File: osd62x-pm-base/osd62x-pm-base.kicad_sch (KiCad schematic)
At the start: 0 parts

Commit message: Schematic update
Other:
- added sheet clocks & reset (clocksresets.kicad_sch)
- added sheet ddr & gpmc interface (ddr-gpmc.kicad_sch)
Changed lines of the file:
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@@
+		)
+	)
+	(sheet
+		(at 25.4 55.88)
+		(size 26.67 6.35)
+		(exclude_from_sim no)
+		(in_bom yes)
+		(on_board yes)
+		(dnp no)
+		(fields_autoplaced yes)
+		(stroke
+			(width 0.1524)
+			(type solid)
+		)
+		(fill
+			(color 0 0 0 0.0000)
+		)
+		(property "Sheetname" "ddr & gpmc interface"
+			(at 25.4 55.1684 0)
+			(effects
+				(font
+					(size 1.27 1.27)
+				)
+				(justify left bottom)
+			)
+		)
+		(property "Sheetfile" "ddr-gpmc.kicad_sch"
+			(at 25.4 62.8146 0)
+			(effects
+				(font
+					(size 1.27 1.27)
+				)
+				(justify left top)
+			)
+		)
+		(instances
+			(project "osd62x-pm-base"
+				(path "/45b90a68-cf5c-4d95-91b2-d04264fee060"
+					(page "4")
+				)
+			)
+		)
+	)
+	(sheet
+		(at 25.4 43.18)
+		(size 26.67 6.35)
+		(exclude_from_sim no)
+		(in_bom yes)
+		(on_board yes)
+		(dnp no)
+		(fields_autoplaced yes)
+		(stroke
+			(width 0.1524)
+			(type solid)
+		)
+		(fill
+			(color 0 0 0 0.0000)
+		)
+		(property "Sheetname" "clocks & reset"
+			(at 25.4 42.4684 0)
+			(effects
+				(font
+					(size 1.27 1.27)
+				)
+				(justify left bottom)
+			)
+		)
+		(property "Sheetfile" "clocksresets.kicad_sch"
+			(at 25.4 50.1146 0)
+			(effects
+				(font
+					(size 1.27 1.27)
+				)
+				(justify left top)
+			)
+		)
+		(instances
+			(project "osd62x-pm-base"
+				(path "/45b90a68-cf5c-4d95-91b2-d04264fee060"
+					(page "3")
+				)
+			)
 		)
 	)

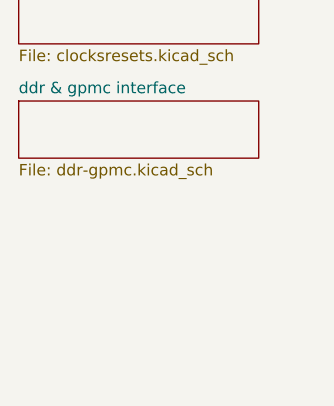
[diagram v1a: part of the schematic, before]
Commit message: Unit D created and peripherals page added
Created unit D and added peripherals schematic page
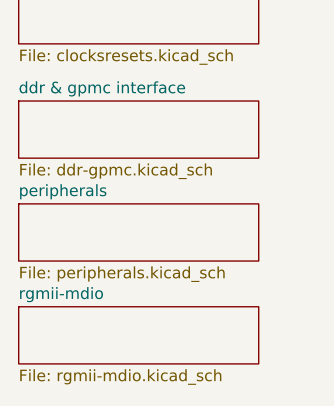
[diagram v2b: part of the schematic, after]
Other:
- added sheet peripherals (peripherals.kicad_sch)
- added sheet rgmii-mdio (rgmii-mdio.kicad_sch)
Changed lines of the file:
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@@
+		)
+	)
+	(sheet
+		(at 25.4 67.31)
+		(size 26.67 6.35)
+		(exclude_from_sim no)
+		(in_bom yes)
+		(on_board yes)
+		(dnp no)
+		(fields_autoplaced yes)
+		(stroke
+			(width 0.1524)
+			(type solid)
+		)
+		(fill
+			(color 0 0 0 0.0000)
+		)
+		(property "Sheetname" "peripherals"
+			(at 25.4 66.5984 0)
+			(effects
+				(font
+					(size 1.27 1.27)
+				)
+				(justify left bottom)
+			)
+		)
+		(property "Sheetfile" "peripherals.kicad_sch"
+			(at 25.4 74.2446 0)
+			(effects
+				(font
+					(size 1.27 1.27)
+				)
+				(justify left top)
+			)
+		)
+		(instances
+			(project "osd62x-pm-base"
+				(path "/45b90a68-cf5c-4d95-91b2-d04264fee060"
+					(page "5")
+				)
+			)
+		)
+	)
+	(sheet
+		(at 25.4 78.74)
+		(size 26.67 6.35)
+		(exclude_from_sim no)
+		(in_bom yes)
+		(on_board yes)
+		(dnp no)
+		(fields_autoplaced yes)
+		(stroke
+			(width 0.1524)
+			(type solid)
+		)
+		(fill
+			(color 0 0 0 0.0000)
+		)
+		(property "Sheetname" "rgmii-mdio"
+			(at 25.4 78.0284 0)
+			(effects
+				(font
+					(size 1.27 1.27)
+				)
+				(justify left bottom)
+			)
+		)
+		(property "Sheetfile" "rgmii-mdio.kicad_sch"
+			(at 25.4 85.6746 0)
+			(effects
+				(font
+					(size 1.27 1.27)
+				)
+				(justify left top)
+			)
+		)
+		(instances
+			(project "osd62x-pm-base"
+				(path "/45b90a68-cf5c-4d95-91b2-d04264fee060"
+					(page "6")
+				)
+			)
 		)
 	)

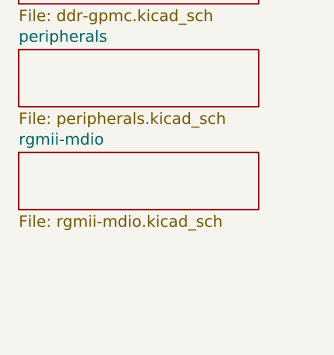
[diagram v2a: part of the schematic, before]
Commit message: Unit F created and placed.
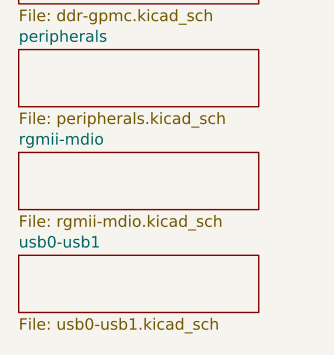
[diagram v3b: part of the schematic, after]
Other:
- added sheet usb0-usb1 (usb0-usb1.kicad_sch)
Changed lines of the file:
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@@
+	)
+	(sheet
+		(at 25.4 90.17)
+		(size 26.67 6.35)
+		(exclude_from_sim no)
+		(in_bom yes)
+		(on_board yes)
+		(dnp no)
+		(fields_autoplaced yes)
+		(stroke
+			(width 0.1524)
+			(type solid)
+		)
+		(fill
+			(color 0 0 0 0.0000)
+		)
+		(property "Sheetname" "usb0-usb1"
+			(at 25.4 89.4584 0)
+			(effects
+				(font
+					(size 1.27 1.27)
+				)
+				(justify left bottom)
+			)
+		)
+		(property "Sheetfile" "usb0-usb1.kicad_sch"
+			(at 25.4 97.1046 0)
+			(effects
+				(font
+					(size 1.27 1.27)
+				)
+				(justify left top)
+			)
+		)
+		(instances
+			(project "osd62x-pm-base"
+				(path "/45b90a68-cf5c-4d95-91b2-d04264fee060"
+					(page "7")
+				)
+			)
+		)
 	)
 	(sheet

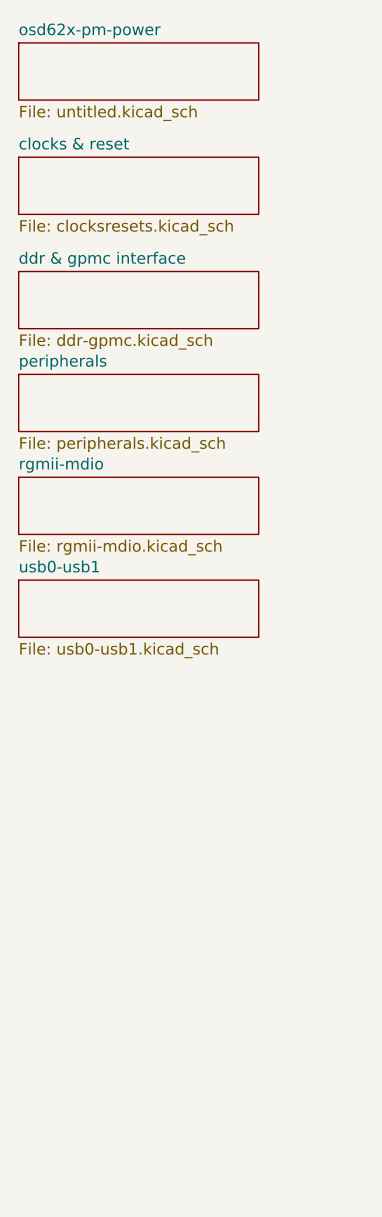
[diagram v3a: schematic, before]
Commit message: Unit G & H added
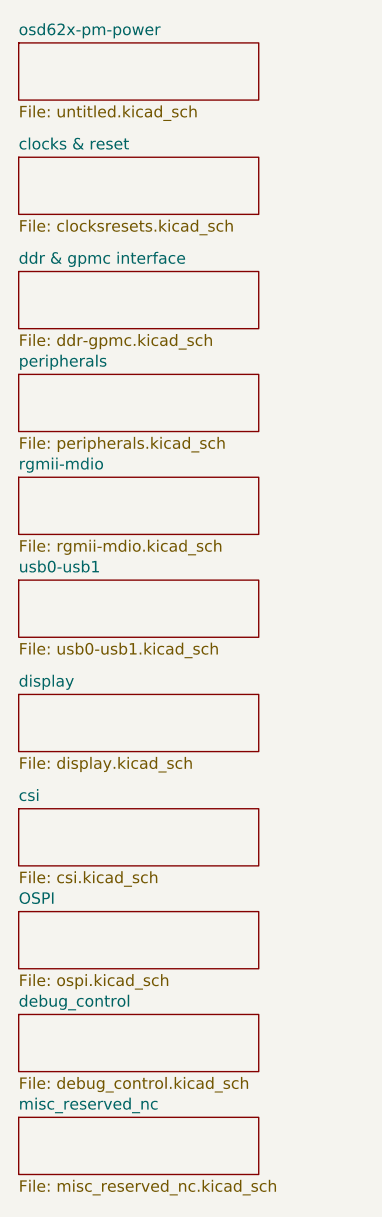
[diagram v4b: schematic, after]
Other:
- added sheet OSPI (ospi.kicad_sch)
- added sheet csi (csi.kicad_sch)
- added sheet debug_control (debug_control.kicad_sch)
- added sheet display (display.kicad_sch)
- added sheet misc_reserved_nc (misc_reserved_nc.kicad_sch)
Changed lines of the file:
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@@
+	)
+	(sheet
+		(at 25.4 115.57)
+		(size 26.67 6.35)
+		(exclude_from_sim no)
+		(in_bom yes)
+		(on_board yes)
+		(dnp no)
+		(fields_autoplaced yes)
+		(stroke
+			(width 0.1524)
+			(type solid)
+		)
+		(fill
+			(color 0 0 0 0.0000)
+		)
+		(property "Sheetname" "csi"
+			(at 25.4 114.8584 0)
+			(effects
+				(font
+					(size 1.27 1.27)
+				)
+				(justify left bottom)
+			)
+		)
+		(property "Sheetfile" "csi.kicad_sch"
+			(at 25.4 122.5046 0)
+			(effects
+				(font
+					(size 1.27 1.27)
+				)
+				(justify left top)
+			)
+		)
+		(instances
+			(project "osd62x-pm-base"
+				(path "/45b90a68-cf5c-4d95-91b2-d04264fee060"
+					(page "9")
+				)
+			)
+		)
+	)
+	(sheet
+		(at 25.4 102.87)
+		(size 26.67 6.35)
+		(exclude_from_sim no)
+		(in_bom yes)
+		(on_board yes)
+		(dnp no)
+		(fields_autoplaced yes)
+		(stroke
+			(width 0.1524)
+			(type solid)
+		)
+		(fill
+			(color 0 0 0 0.0000)
+		)
+		(property "Sheetname" "display"
+			(at 25.4 102.1584 0)
+			(effects
+				(font
+					(size 1.27 1.27)
+				)
+				(justify left bottom)
+			)
+		)
+		(property "Sheetfile" "display.kicad_sch"
+			(at 25.4 109.8046 0)
+			(effects
+				(font
+					(size 1.27 1.27)
+				)
+				(justify left top)
+			)
+		)
+		(instances
+			(project "osd62x-pm-base"
+				(path "/45b90a68-cf5c-4d95-91b2-d04264fee060"
+					(page "8")
+				)
+			)
+		)
 	)
 	(sheet
@@
 	)
 	(sheet
+		(at 25.4 138.43)
+		(size 26.67 6.35)
+		(exclude_from_sim no)
+		(in_bom yes)
+		(on_board yes)
+		(dnp no)
+		(fields_autoplaced yes)
+		(stroke
+			(width 0.1524)
+			(type solid)
+		)
+		(fill
+			(color 0 0 0 0.0000)
+		)
+		(property "Sheetname" "debug_control"
+			(at 25.4 137.7184 0)
+			(effects
+				(font
+					(size 1.27 1.27)
+				)
+				(justify left bottom)
+			)
+		)
+		(property "Sheetfile" "debug_control.kicad_sch"
+			(at 25.4 145.3646 0)
+			(effects
+				(font
+					(size 1.27 1.27)
+				)
+				(justify left top)
+			)
+		)
+		(instances
+			(project "osd62x-pm-base"
+				(path "/45b90a68-cf5c-4d95-91b2-d04264fee060"
+					(page "11")
+				)
+			)
+		)
+	)
+	(sheet
+		(at 25.4 149.86)
+		(size 26.67 6.35)
+		(exclude_from_sim no)
+		(in_bom yes)
+		(on_board yes)
+		(dnp no)
+		(fields_autoplaced yes)
+		(stroke
+			(width 0.1524)
+			(type solid)
+		)
+		(fill
+			(color 0 0 0 0.0000)
+		)
+		(property "Sheetname" "misc_reserved_nc"
+			(at 25.4 149.1484 0)
+			(effects
+				(font
+					(size 1.27 1.27)
+				)
+				(justify left bottom)
+			)
+		)
+		(property "Sheetfile" "misc_reserved_nc.kicad_sch"
+			(at 25.4 156.7946 0)
+			(effects
+				(font
+					(size 1.27 1.27)
+				)
+				(justify left top)
+			)
+		)
+		(instances
+			(project "osd62x-pm-base"
+				(path "/45b90a68-cf5c-4d95-91b2-d04264fee060"
+					(page "12")
+				)
+			)
+		)
+	)
+	(sheet
 		(at 25.4 43.18)
 		(size 26.67 6.35)
@@
 				)
 			)
+		)
+	)
+	(sheet
+		(at 25.4 127)
+		(size 26.67 6.35)
+		(exclude_from_sim no)
+		(in_bom yes)
+		(on_board yes)
+		(dnp no)
+		(fields_autoplaced yes)
+		(stroke
+			(width 0.1524)
+			(type solid)
+		)
+		(fill
+			(color 0 0 0 0.0000)
+		)
+		(property "Sheetname" "OSPI"
+			(at 25.4 126.2884 0)
+			(effects
+				(font
+					(size 1.27 1.27)
+				)
+				(justify left bottom)
+			)
+		)
+		(property "Sheetfile" "ospi.kicad_sch"
+			(at 25.4 133.9346 0)
+			(effects
+				(font
+					(size 1.27 1.27)
+				)
+				(justify left top)
+			)
+		)
+		(instances
+			(project "osd62x-pm-base"
+				(path "/45b90a68-cf5c-4d95-91b2-d04264fee060"
+					(page "10")
+				)
+			)
